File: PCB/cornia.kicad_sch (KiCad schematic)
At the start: 65 parts, among them SW1 SW_Push, SW10 SW_Push, SW11 SW_Push, SW12 SW_Push, SW13 SW_Push, SW14 SW_Push, SW15 SW_Push, SW16 SW_Push, SW17 SW_Push, SW18 SW_Push, SW19 SW_Push, SW2 SW_Push, SW20 SW_Push, SW21 SW_Push, SW3 SW_Push, SW4 SW_Push, SW5 SW_Push, SW6 SW_Push, SW7 SW_Push, SW8 SW_Push, SW9 SW_Push, U1 RP2040-ProMicro, U2 TRRS

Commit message: [PCB] Add handedness pin
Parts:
- added R5, R6: 2.2k, cornia-footprints:R_0805, symbol Device:R
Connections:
- net GND: now also R6.2
- net VBUS: now also R5.1
- new net Handedness: R5.2, R6.1, U1.32 (25)
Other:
- note added: "Left (B.Cu)"
- note added: "Right (F.Cu)"
- moved on the sheet: C1, H1, H2, H3, H4, H5, H6, L1, L10, L11, L12, L13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

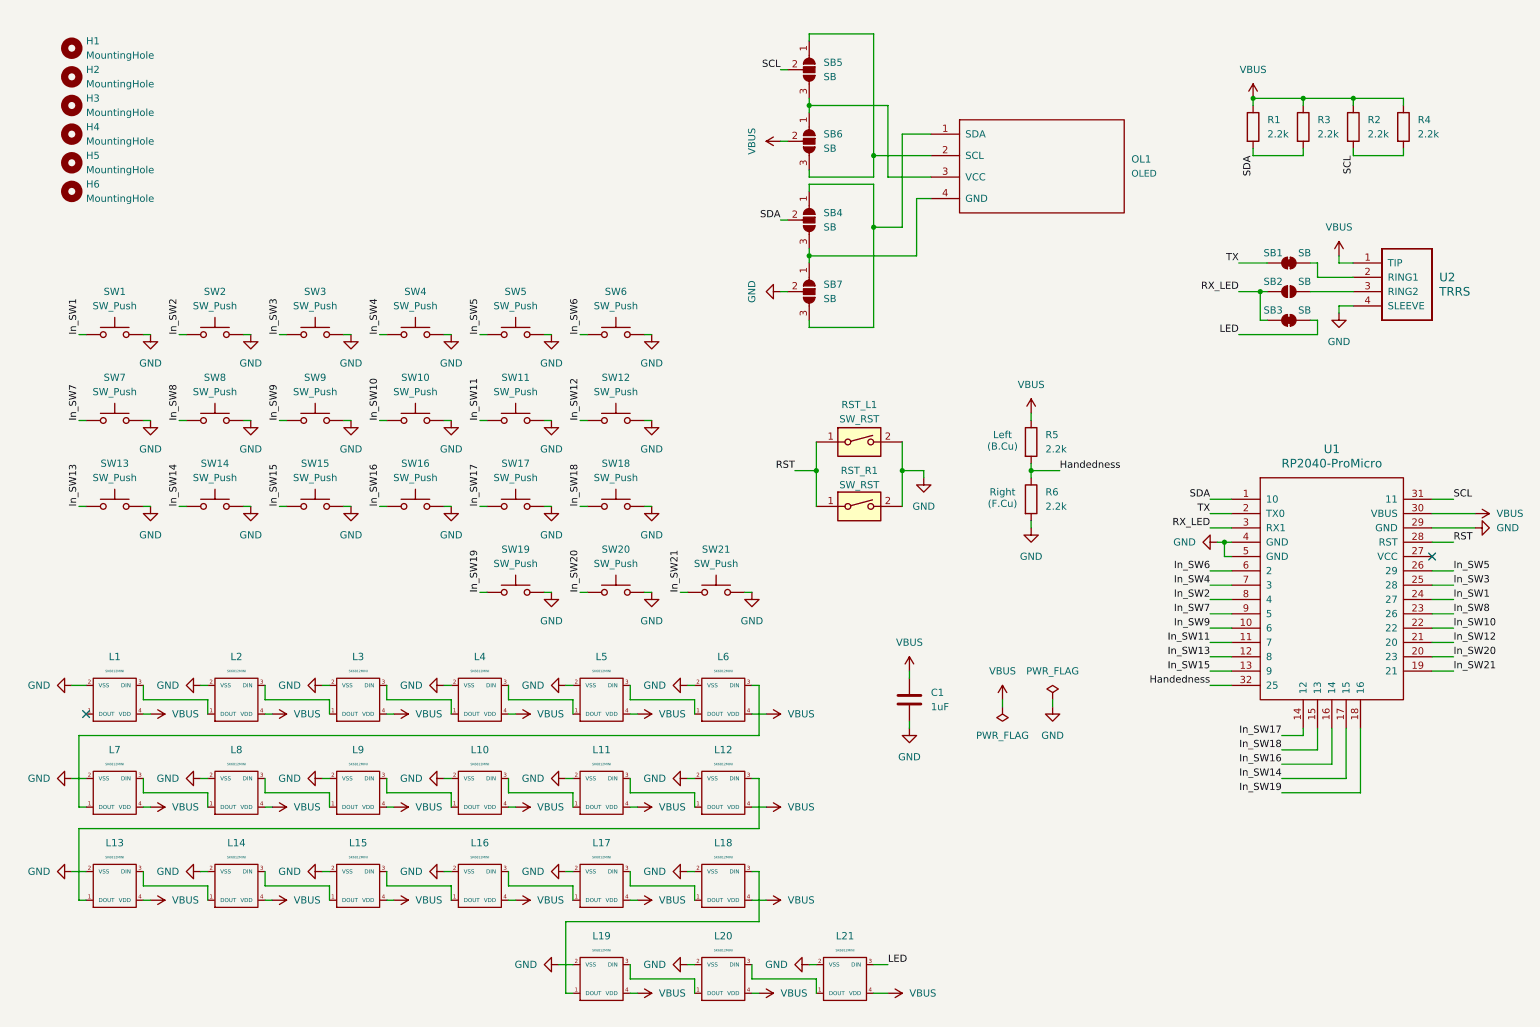
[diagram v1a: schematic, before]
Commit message: [PCB] Rework OLED SBx & Add last led DOUT TP
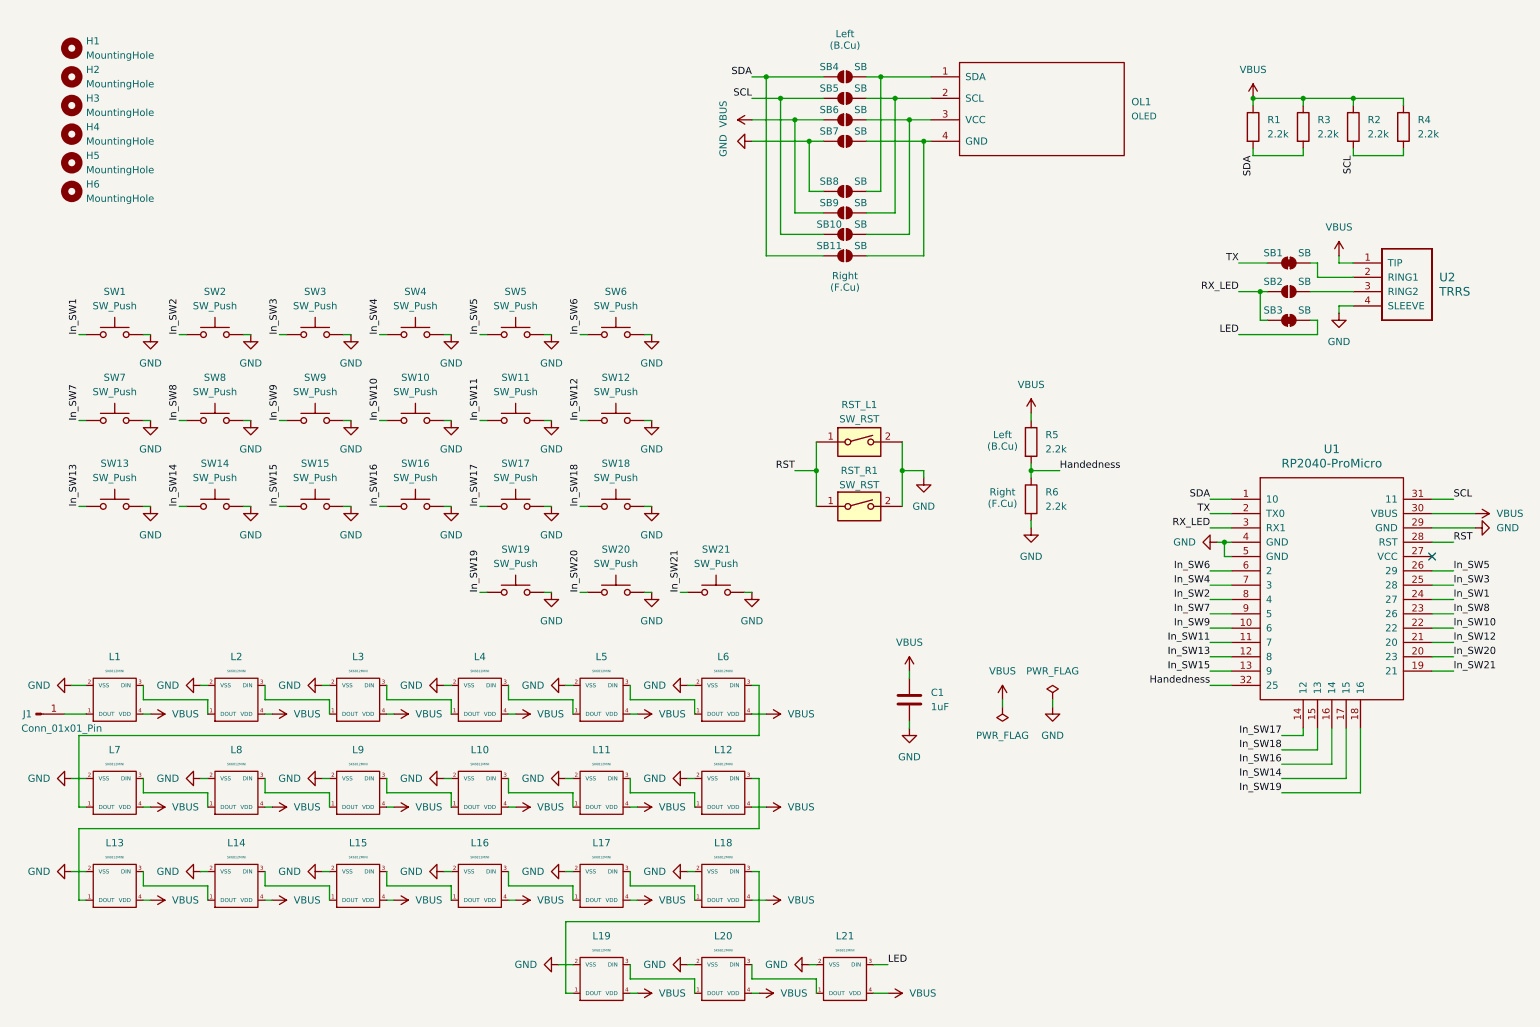
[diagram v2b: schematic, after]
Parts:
- removed SB4, SB5, SB6, SB7: SB, cornia-footprints:SolderJumper-3, symbol Jumper:SolderJumper_3_Open
- added J1: Conn_01x01_Pin, cornia-footprints:1Pin, symbol Connector:Conn_01x01_Pin
- added SB10, SB11, SB4, SB5, SB6, SB7, SB8, SB9: SB, cornia-footprints:SolderJumper-2_Open, symbol Jumper:SolderJumper_2_Open
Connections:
- net GND: now also SB7.1 (A), SB8.1 (A)
- net SCL: now also SB10.1 (A), SB5.1 (A)
- net SDA: now also SB11.1 (A), SB4.1 (A)
- net VBUS: now also SB6.1 (A), SB9.1 (A)
- net at OL1.4 (GND): now also SB11.2 (B), SB7.2 (B)
- net at OL1.1 (SDA): now also SB4.2 (B), SB8.2 (B)
- net at OL1.2 (SCL): now also SB5.2 (B), SB9.2 (B)
- net at OL1.3 (VCC): now also SB10.2 (B), SB6.2 (B)
- net at L1.1 (DOUT): now also J1.1 (Pin_1)
- no-connect marks 2 -> 1
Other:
- moved on the sheet: OL1

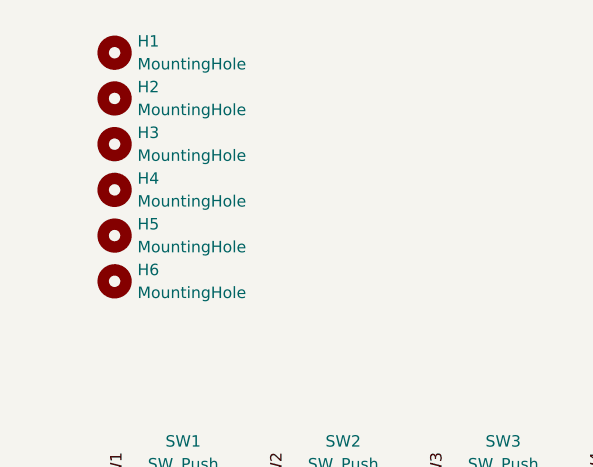
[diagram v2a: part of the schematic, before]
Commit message: [PCB/Footprint] Remove 5mm mounting hole + update RP2040 & RST 3D
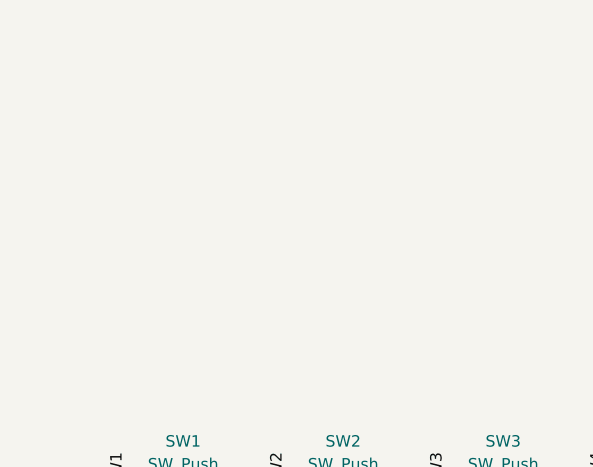
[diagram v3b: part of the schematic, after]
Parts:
- removed H1, H2, H3, H4, H5, H6: MountingHole, cornia-footprints:MountingHole_5mm, symbol Mechanical:MountingHole

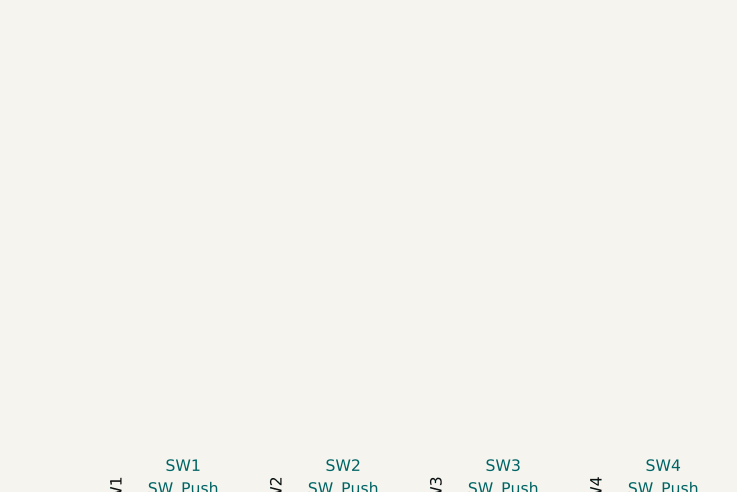
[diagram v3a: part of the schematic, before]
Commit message: [PCB/Symbol] Add 10x 2.2mm holes + Add new logo
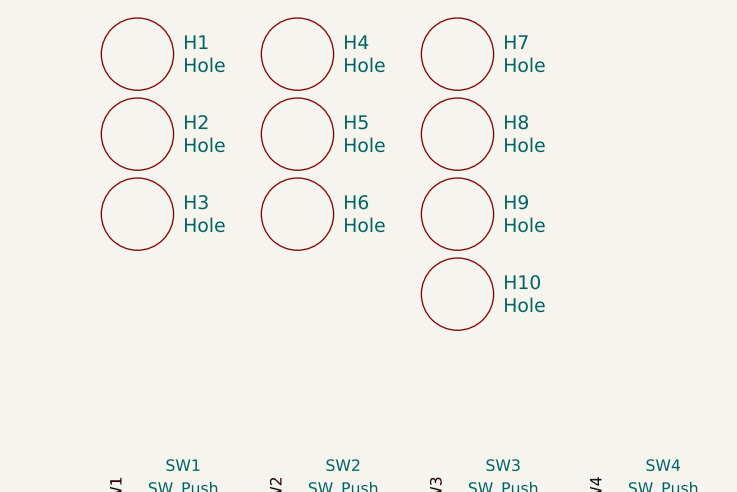
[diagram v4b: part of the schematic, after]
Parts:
- added H1, H10, H2, H3, H4, H5, H6, H7, H8, H9: Hole, cornia-footprints:MountingHole_2.2mm_M2_no_annular, symbol cornia:Hole

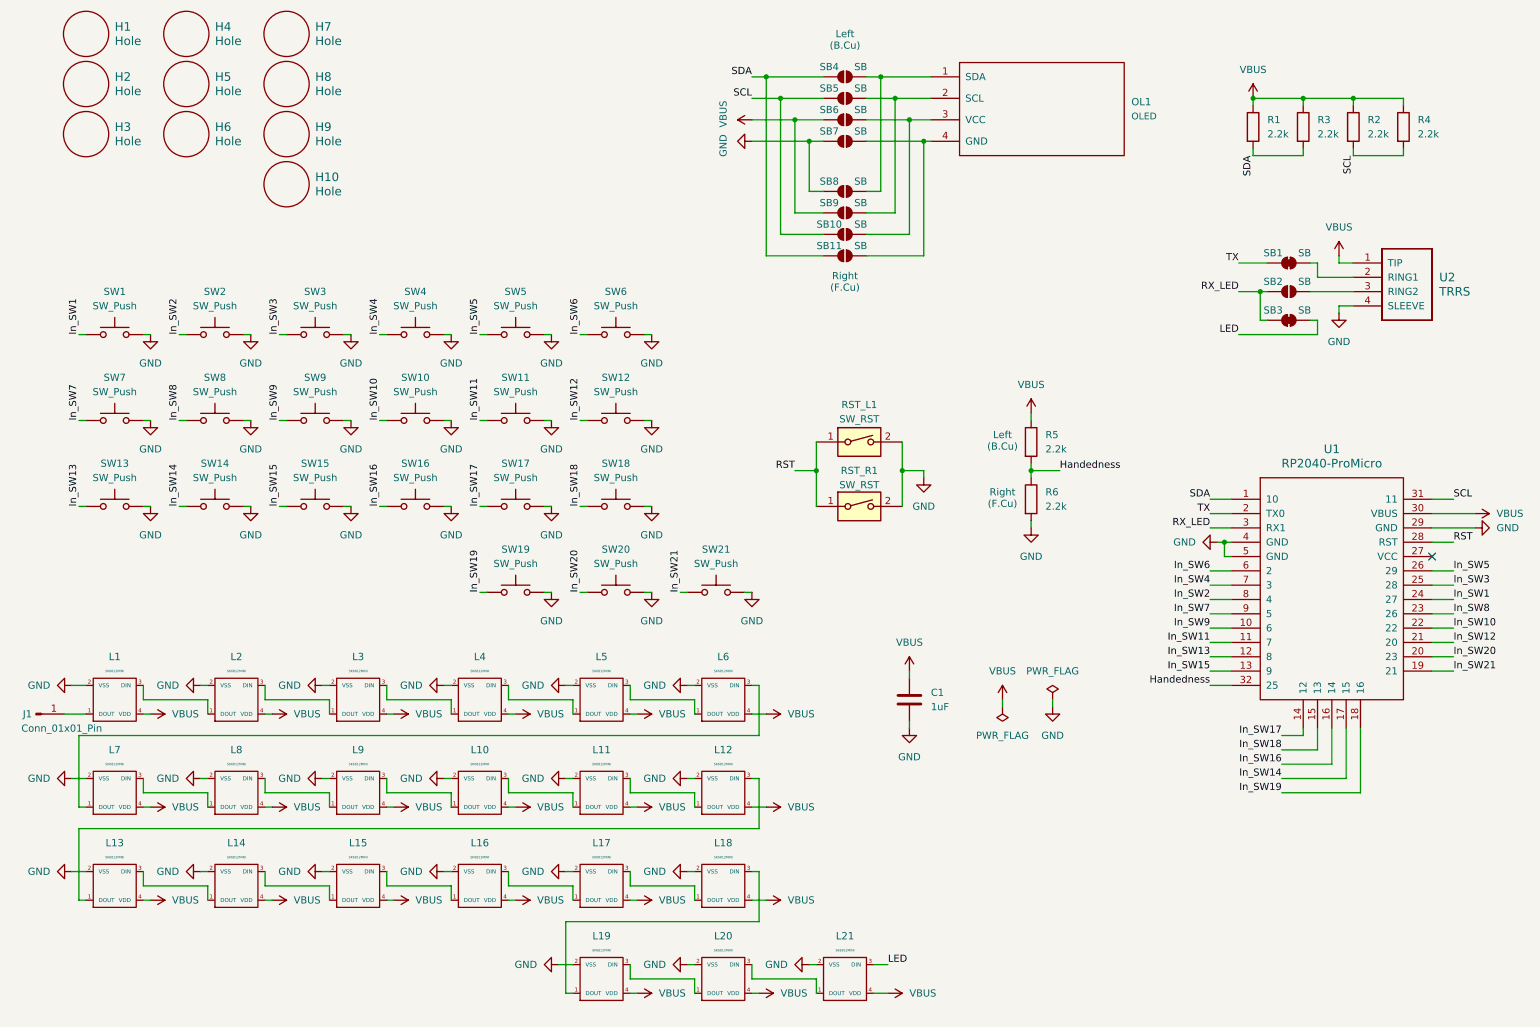
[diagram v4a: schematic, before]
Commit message: [PCB] Fix RGB Led pin assignment mistake
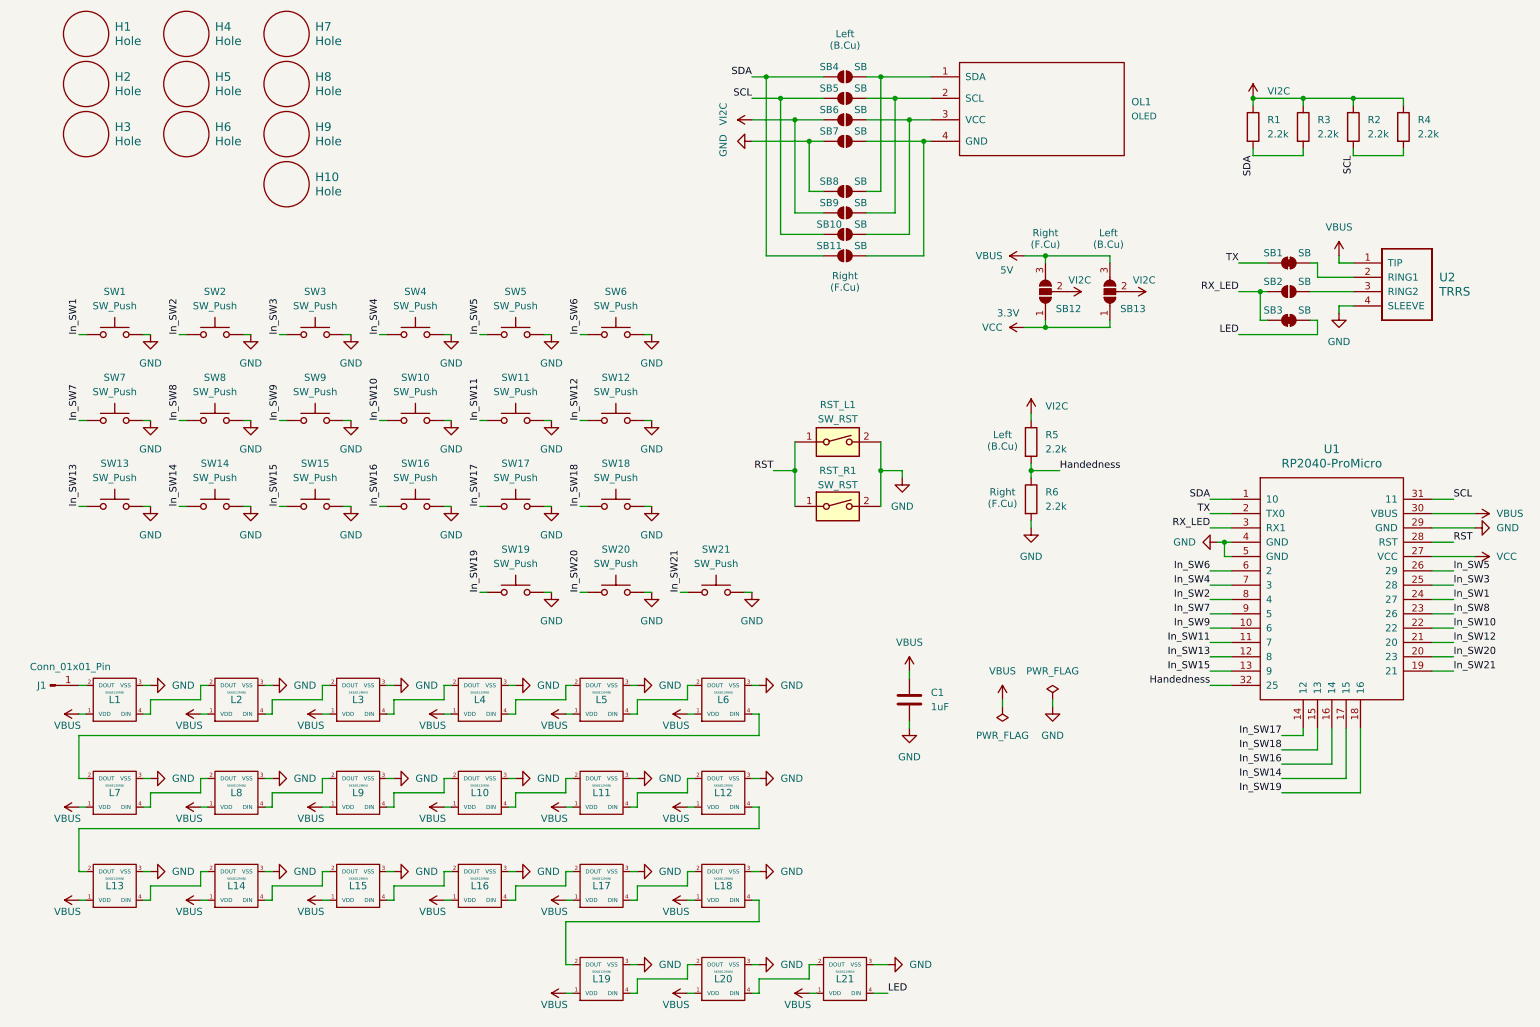
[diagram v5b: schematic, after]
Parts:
- added SB12, SB13: SolderJumper_3_Open, cornia-footprints:SolderJumper-3_I2C, symbol Jumper:SolderJumper_3_Open
- SB10, SB11, SB4, SB5, SB6, SB7, SB8, SB9: footprint cornia-footprints:SolderJumper-2_Open -> cornia-footprints:SolderJumper-2_Open_NoSilk
- U2: footprint cornia-footprints:TRRS -> cornia-footprints:TRRS_PJ-320A
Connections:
- net GND: now also L1.3 (VSS), L10.3 (VSS), L11.3 (VSS), L12.3 (VSS), L13.3 (VSS), L14.3 (VSS), L15.3 (VSS), L16.3 (VSS), L17.3 (VSS), L18.3 (VSS), L19.3 (VSS), L2.3 (VSS), L20.3 (VSS), L21.3 (VSS), L3.3 (VSS), L4.3 (VSS), L5.3 (VSS), L6.3 (VSS), L7.3 (VSS), L8.3 (VSS), L9.3 (VSS); no longer L1.2 (VSS), L10.2 (VSS), L11.2 (VSS), L12.2 (VSS), L13.2 (VSS), L14.2 (VSS), L15.2 (VSS), L16.2 (VSS), L17.2 (VSS), L18.2 (VSS), L19.2 (VSS), L2.2 (VSS), L20.2 (VSS), L21.2 (VSS), L3.2 (VSS), L4.2 (VSS), L5.2 (VSS), L6.2 (VSS), L7.2 (VSS), L8.2 (VSS), L9.2 (VSS)
- net LED: now also L21.4 (DIN); no longer L21.3 (DIN)
- net VBUS: now also L1.1 (VDD), L10.1 (VDD), L11.1 (VDD), L12.1 (VDD), L13.1 (VDD), L14.1 (VDD), L15.1 (VDD), L16.1 (VDD), L17.1 (VDD), L18.1 (VDD), L19.1 (VDD), L2.1 (VDD), L20.1 (VDD), L21.1 (VDD), L3.1 (VDD), L4.1 (VDD), L5.1 (VDD), L6.1 (VDD), L7.1 (VDD), L8.1 (VDD), L9.1 (VDD), SB12.3 (B), SB13.3 (B); no longer L1.4 (VDD), L10.4 (VDD), L11.4 (VDD), L12.4 (VDD), L13.4 (VDD), L14.4 (VDD), L15.4 (VDD), L16.4 (VDD), L17.4 (VDD), L18.4 (VDD), L19.4 (VDD), L2.4 (VDD), L20.4 (VDD), L21.4 (VDD), L3.4 (VDD), L4.4 (VDD), L5.4 (VDD), L6.4 (VDD), L7.4 (VDD), L8.4 (VDD), L9.4 (VDD), R1.1, R2.1, R3.1, R4.1, R5.1, SB6.1 (A), SB9.1 (A)
- net VCC: now reaches U1.27 (VCC)
- net VCC: now also SB12.1 (A), SB13.1 (A)
- net at J1.1 (Pin_1): now also L1.2 (DOUT); no longer L1.1 (DOUT)
- new net: L2.4 (DIN), L3.2 (DOUT)
- new net: L3.4 (DIN), L4.2 (DOUT)
- new net: L10.4 (DIN), L11.2 (DOUT)
- new net: L11.4 (DIN), L12.2 (DOUT)
- new net: L18.4 (DIN), L19.2 (DOUT)
- new net: L19.4 (DIN), L20.2 (DOUT)
- new net: L8.4 (DIN), L9.2 (DOUT)
- new net: L10.2 (DOUT), L9.4 (DIN)
- new net: L14.4 (DIN), L15.2 (DOUT)
- new net: L15.4 (DIN), L16.2 (DOUT)
- new net: L7.4 (DIN), L8.2 (DOUT)
- new net: L12.4 (DIN), L13.2 (DOUT)
- new net: L16.4 (DIN), L17.2 (DOUT)
- new net: L17.4 (DIN), L18.2 (DOUT)
- new net: L5.4 (DIN), L6.2 (DOUT)
- new net: L6.4 (DIN), L7.2 (DOUT)
- new net: L20.4 (DIN), L21.2 (DOUT)
- new net: L4.4 (DIN), L5.2 (DOUT)
- new net: L13.4 (DIN), L14.2 (DOUT)
- new net: L1.4 (DIN), L2.2 (DOUT)
- new net VI2C: R1.1, R2.1, R3.1, R4.1, R5.1, SB12.2 (C), SB13.2 (C), SB6.1 (A), SB9.1 (A)
- no-connect marks 1 -> 0
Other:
- note added: "3.3V"
- note added: "5V"
- title: (none) -> Cornia
- moved on the sheet: RST_L1, RST_R1
